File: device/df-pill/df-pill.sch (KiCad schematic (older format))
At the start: 58 parts, among them J1 USB_B_Micro, P1 Connector_A, P2 Connector_B, P3 Connector_SWD, SW1 RESET, SW2 KEY, U1 MIC5219-3.3YM5, U2 STM32F103C8Tx, U3 USBLC6-2SC6, Y1 8MHz, Y2 32.768KHz

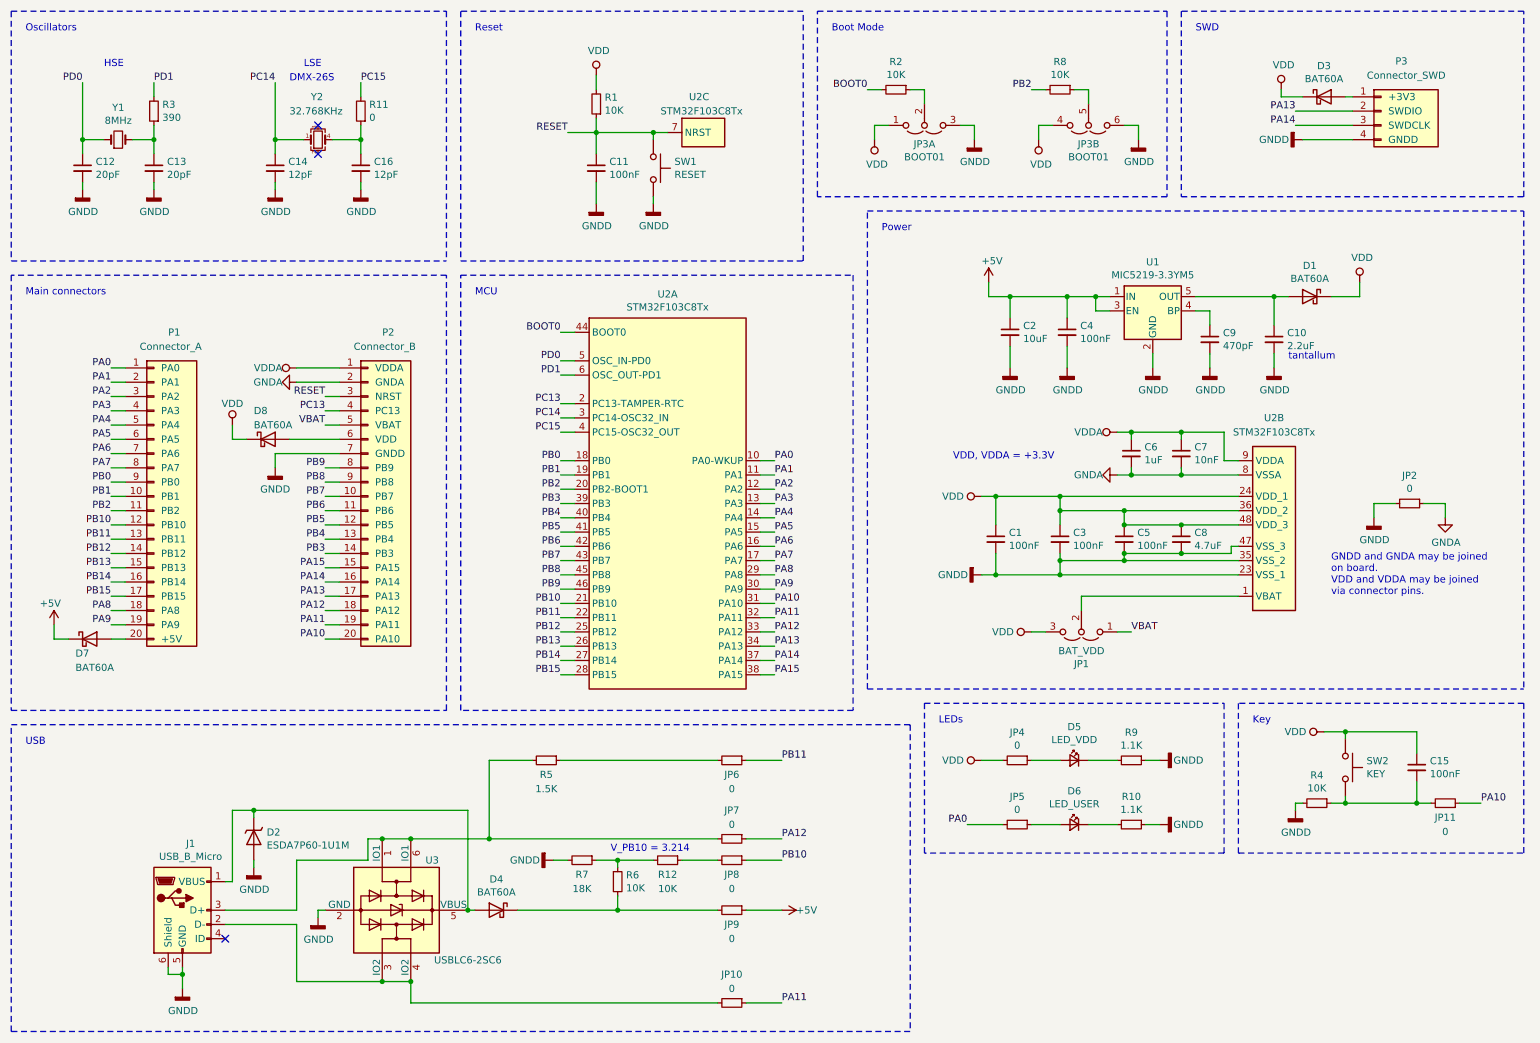
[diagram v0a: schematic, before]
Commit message: rev.1.3.0
Fix schematic symbols and footprints to point to local library
Fix D4 position
Add R13 as a jumper for separating PC14 from LSE
Change Key from pull-down to pull-up
Remove C15 in favor of software debouncing for Key
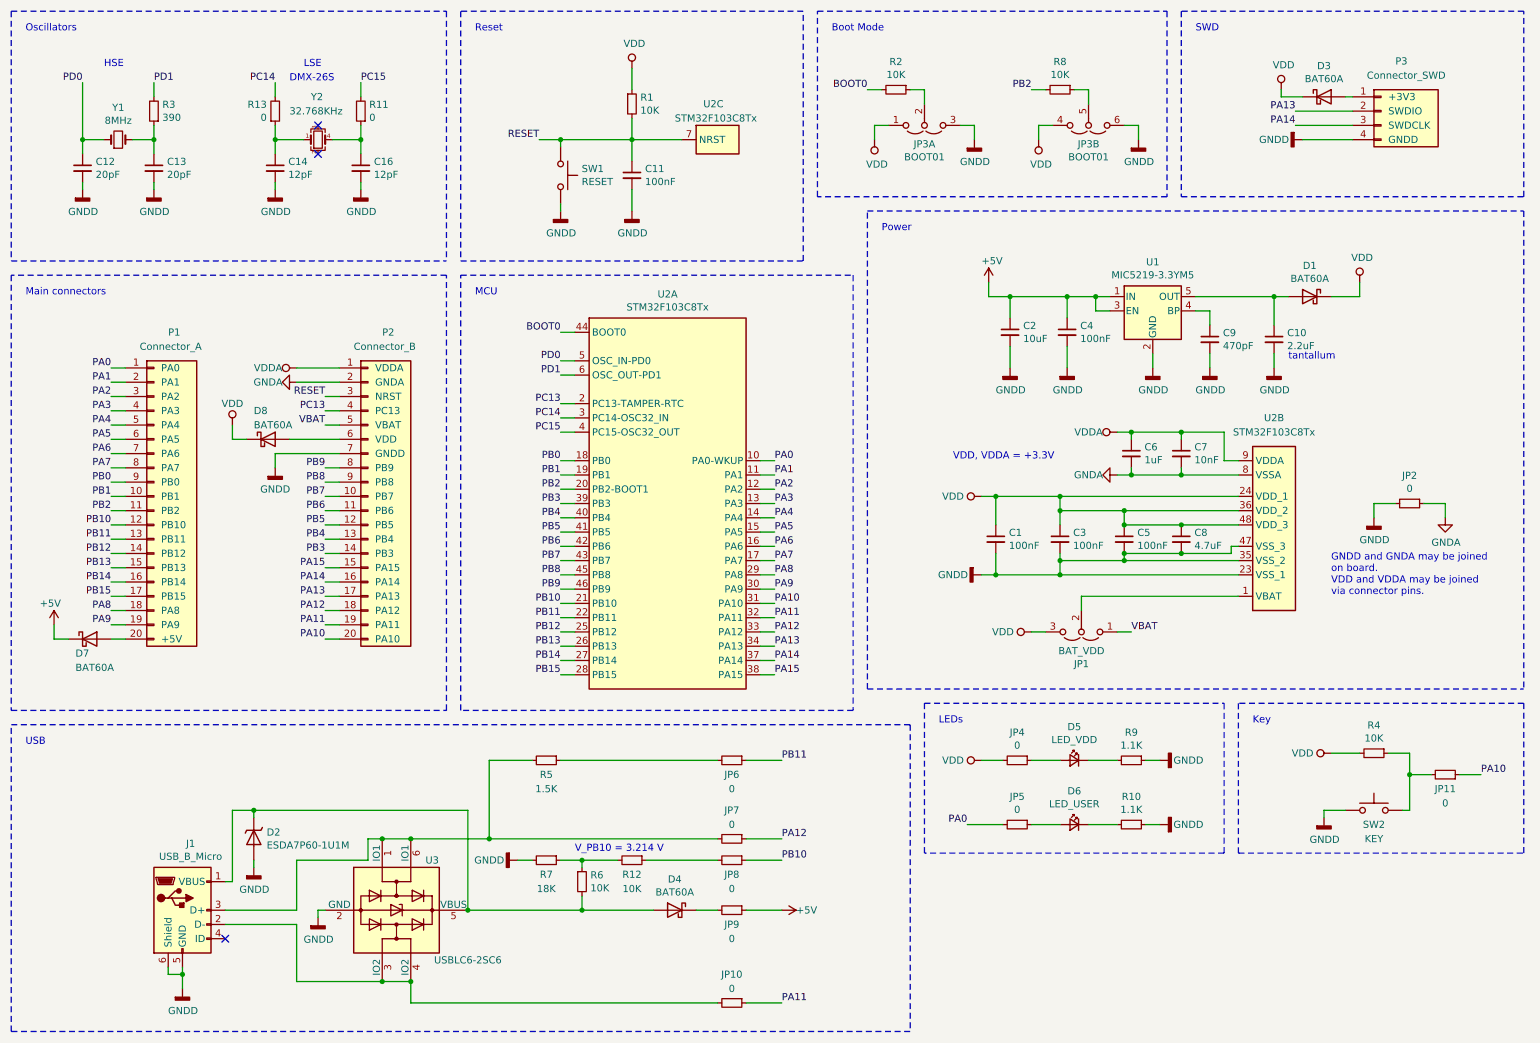
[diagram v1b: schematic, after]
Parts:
- removed C15: 100nF, fp:C_0603_1608Metric, symbol sym:C_Small
- added R13: 0, fp:R_0603_1608Metric, symbol sym:R_Small
- D7, D8: footprint Diode_SMD:D_SOD-323 -> fp:D_SOD-323
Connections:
- net GNDD: now also SW2.1; no longer R4.2
- net PC14: now also R13.2; no longer C14.1, Y2.1
- net RESET: now also R1.2; no longer R1.1
- net VDD: now also R1.1, R4.2; no longer R1.2, SW2.1
- net at D2.1 (A1), D4.2 (A), J1.1 (VBUS)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: now also R6.2
- net at D4.1 (K), JP9.2: no longer R6.2
- new net: C14.1, R13.1, Y2.1
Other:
- note added: "V_PB10 = 3.214 V"
- note removed: "V_PB10 = 3.214"
- moved on the sheet: C11, D4, JP11, R12, R4, R6, R7, SW1, SW2, U2C
